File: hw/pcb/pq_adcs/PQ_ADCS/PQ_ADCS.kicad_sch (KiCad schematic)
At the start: 57 parts, among them IC2 TMUX1108RSVR, IC3 SN74AUP1G08DBVT, J1 Conn_01x10_MountingPin, J10 Conn_01x11_MountingPin, J2 Conn_01x10_MountingPin, J3 Conn_01x11_MountingPin, J4 CES-110-02-L-S, J5 CES-110-02-L-S, J6 CES-110-02-L-S, J7 CES-110-02-L-S, J8 Conn_01x10_MountingPin, J9 Conn_01x10_MountingPin, U1 MMC5983MA, U2 LT6005CDHC#TRPBF, U3 PCA9547BS,118, U5 LT6004IMS8#PBF

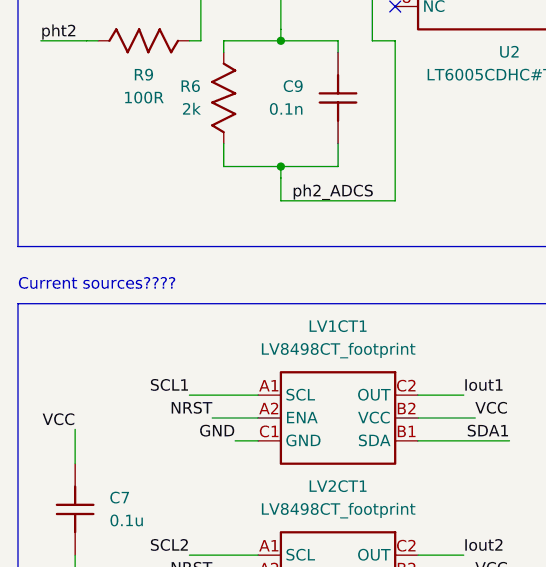
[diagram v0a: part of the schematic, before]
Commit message: identified magnetorquer actuators
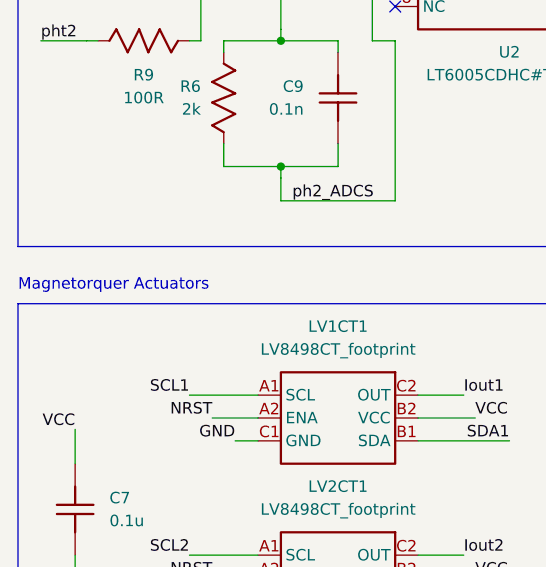
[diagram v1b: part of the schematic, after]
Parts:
- H1: footprint (none) -> MountingHole:MountingHole_3.2mm_M3_Pad
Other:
- note added: "Magnetorquer Actuators"
- note removed: "Current sources????"
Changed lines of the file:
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@@
     (effects (font (size 1.27 1.27)) (justify left bottom))
   )
-  (text "Current sources????" (at 41.91 129.54 0)
+  (text "Magnetorquer Actuators" (at 41.91 129.54 0)
     (effects (font (size 1.27 1.27)) (justify left bottom))
   )
@@
       (effects (font (size 1.27 1.27)) (justify left) hide)
     )
-    (property "Footprint" "" (id 2) (at 245.11 260.35 0)
-      (effects (font (size 1.27 1.27)) hide)
-    )
+    (property "Footprint" "MountingHole:MountingHole_3.2mm_M3_Pad" (id 2) (at 245.11 260.35 0)
+      (effects (font (size 1.27 1.27)) hide)
+    )
